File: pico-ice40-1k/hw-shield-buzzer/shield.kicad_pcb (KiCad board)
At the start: 2 copper layers, 53.3 x 53.8 mm, 30 parts, among them J1 JACK_TRS_6PINS, P1 CONN_12, P2 CONN_12, P3 CONN_01X02, SW2 SW_PUSH, U1 TLV320DAC3203, U2 LD39015M18R, U3 TPA2005D1

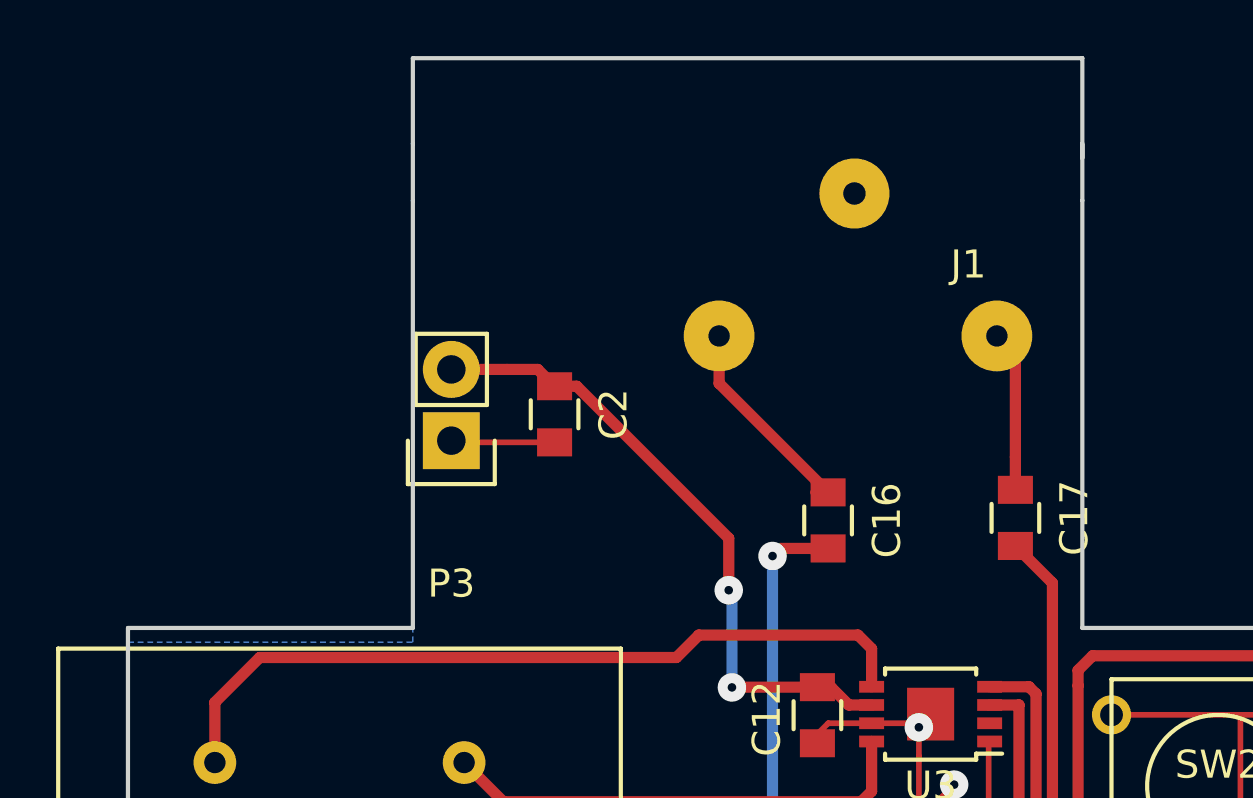
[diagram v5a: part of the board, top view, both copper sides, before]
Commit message: Modif 2 pins header position
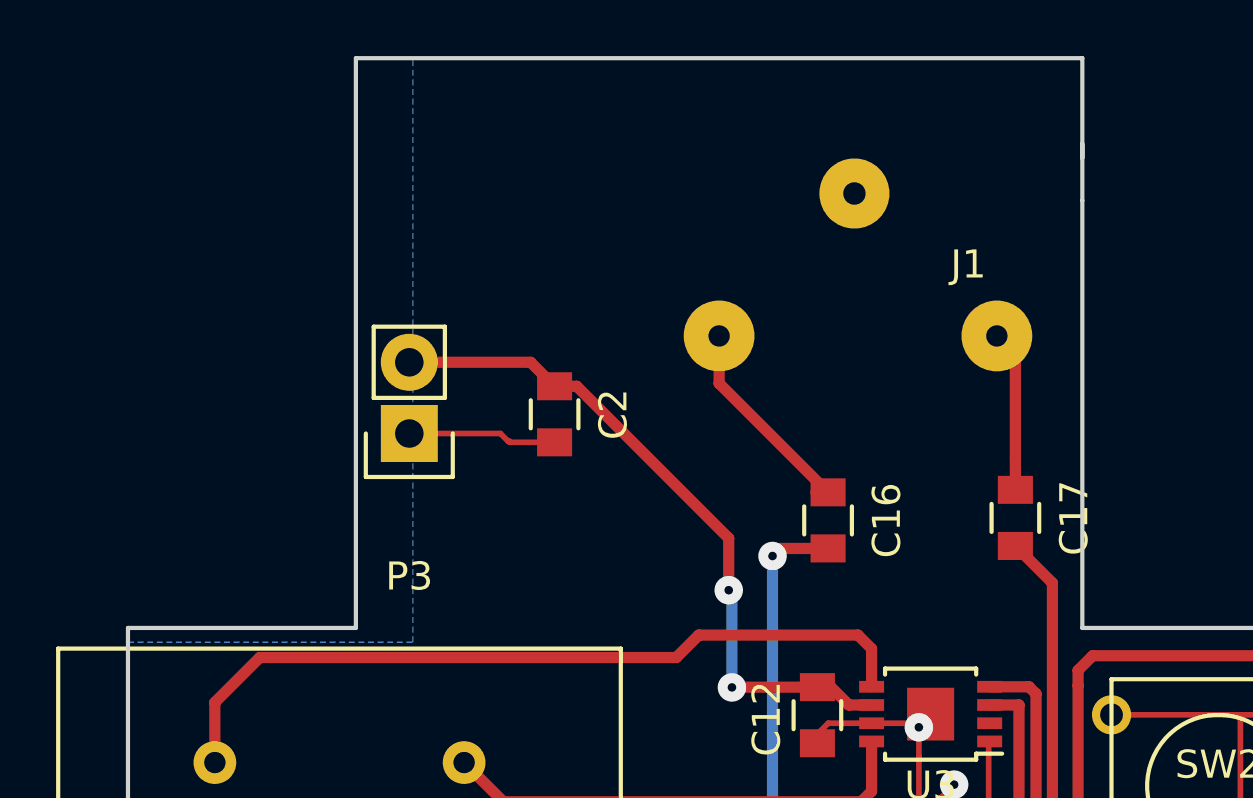
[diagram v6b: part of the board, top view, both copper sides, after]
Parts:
- moved P3 1.52 mm to (155.8, 63.7)
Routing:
- net GND: track 83.5 -> 85.1 mm
- net +5V: track 23.0 -> 24.6 mm
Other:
- outline, holes or cut-outs redrawn
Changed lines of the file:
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@@
   (general
     (links 82)
-    (no_connects 0)
-    (area 145.720999 50.216999 199.211001 104.215001)
+    (no_connects 1)
+    (area 143.079399 48.540599 200.164662 112.781)
     (thickness 1.6)
-    (drawings 16)
-    (tracks 500)
+    (drawings 19)
+    (tracks 502)
     (zones 0)
     (modules 30)
@@
   (layers
     (0 F.Cu signal)
-    (31 B.Cu signal)
+    (31 B.Cu signal hide)
     (32 B.Adhes user)
     (33 F.Adhes user)
@@
     (add_net "Net-(SP1-Pad2)")
   )
+  (module Pin_Headers:Pin_Header_Straight_1x02 locked (layer F.Cu)
+    (at 155.829 63.6778 180)
+    (descr "Through hole pin header")
+    (tags "pin header")
+    (fp_text reference P3 (at 0 -5.1 180) (layer F.SilkS)
+      (effects (font (size 1 1) (thickness 0.15)))
+    )
+    (fp_text value CONN_01X02 (at 0 -3.1 180) (layer F.Fab)
+      (effects (font (size 1 1) (thickness 0.15)))
+    )
+    (fp_line (start 1.27 1.27) (end 1.27 3.81) (layer F.SilkS) (width 0.15))
+    (fp_line (start 1.55 -1.55) (end 1.55 0) (layer F.SilkS) (width 0.15))
+    (fp_line (start -1.75 -1.75) (end -1.75 4.3) (layer F.CrtYd) (width 0.05))
+    (fp_line (start 1.75 -1.75) (end 1.75 4.3) (layer F.CrtYd) (width 0.05))
+    (fp_line (start -1.75 -1.75) (end 1.75 -1.75) (layer F.CrtYd) (width 0.05))
+    (fp_line (start -1.75 4.3) (end 1.75 4.3) (layer F.CrtYd) (width 0.05))
+    (fp_line (start 1.27 1.27) (end -1.27 1.27) (layer F.SilkS) (width 0.15))
+    (fp_line (start -1.55 0) (end -1.55 -1.55) (layer F.SilkS) (width 0.15))
+    (fp_line (start -1.55 -1.55) (end 1.55 -1.55) (layer F.SilkS) (width 0.15))
+    (fp_line (start -1.27 1.27) (end -1.27 3.81) (layer F.SilkS) (width 0.15))
+    (fp_line (start -1.27 3.81) (end 1.27 3.81) (layer F.SilkS) (width 0.15))
+    (pad 1 thru_hole rect (at 0 0 180) (size 2.032 2.032) (drill 1.016) (layers *.Cu *.Mask F.SilkS)
+      (net 2 GND))
+    (pad 2 thru_hole oval (at 0 2.54 180) (size 2.032 2.032) (drill 1.016) (layers *.Cu *.Mask F.SilkS)
+      (net 36 +5V))
+    (model Pin_Headers.3dshapes/Pin_Header_Straight_1x02.wrl
+      (at (xyz 0 -0.05 0))
+      (scale (xyz 1 1 1))
+      (rotate (xyz 0 0 90))
+    )
+  )
   (module Capacitors_SMD:C_0805 placed (layer F.Cu)
     (at 171.45 93.9292)
@@
     )
   )
-  (module Pin_Headers:Pin_Header_Straight_1x02 locked (layer F.Cu)
-    (at 157.3276 63.9318 180)
-    (descr "Through hole pin header")
-    (tags "pin header")
-    (fp_text reference P3 (at 0 -5.1 180) (layer F.SilkS)
-      (effects (font (size 1 1) (thickness 0.15)))
-    )
-    (fp_text value CONN_01X02 (at 0 -3.1 180) (layer F.Fab)
-      (effects (font (size 1 1) (thickness 0.15)))
-    )
-    (fp_line (start 1.27 1.27) (end 1.27 3.81) (layer F.SilkS) (width 0.15))
-    (fp_line (start 1.55 -1.55) (end 1.55 0) (layer F.SilkS) (width 0.15))
-    (fp_line (start -1.75 -1.75) (end -1.75 4.3) (layer F.CrtYd) (width 0.05))
-    (fp_line (start 1.75 -1.75) (end 1.75 4.3) (layer F.CrtYd) (width 0.05))
-    (fp_line (start -1.75 -1.75) (end 1.75 -1.75) (layer F.CrtYd) (width 0.05))
-    (fp_line (start -1.75 4.3) (end 1.75 4.3) (layer F.CrtYd) (width 0.05))
-    (fp_line (start 1.27 1.27) (end -1.27 1.27) (layer F.SilkS) (width 0.15))
-    (fp_line (start -1.55 0) (end -1.55 -1.55) (layer F.SilkS) (width 0.15))
-    (fp_line (start -1.55 -1.55) (end 1.55 -1.55) (layer F.SilkS) (width 0.15))
-    (fp_line (start -1.27 1.27) (end -1.27 3.81) (layer F.SilkS) (width 0.15))
-    (fp_line (start -1.27 3.81) (end 1.27 3.81) (layer F.SilkS) (width 0.15))
-    (pad 1 thru_hole rect (at 0 0 180) (size 2.032 2.032) (drill 1.016) (layers *.Cu *.Mask F.SilkS)
-      (net 2 GND))
-    (pad 2 thru_hole oval (at 0 2.54 180) (size 2.032 2.032) (drill 1.016) (layers *.Cu *.Mask F.SilkS)
-      (net 36 +5V))
-    (model Pin_Headers.3dshapes/Pin_Header_Straight_1x02.wrl
-      (at (xyz 0 -0.05 0))
-      (scale (xyz 1 1 1))
-      (rotate (xyz 0 0 90))
-    )
-  )
   (module Capacitors_SMD:C_0805 (layer F.Cu)
     (at 170.3832 73.7235 270)
@@
     )
   )
-  (gr_line (start 155.956 55.372) (end 155.956 70.612) (angle 90) (layer Edge.Cuts) (width 0.15))
+  (dimension 40.728932 (width 0.3) (layer Eco1.User)
+    (gr_text "40,729 mm" (at 176.165621 41.340258 0.07146336115) (layer Eco1.User)
+      (effects (font (size 1.5 1.5) (thickness 0.3)))
+    )
+    (feature1 (pts (xy 196.5579 63.627) (xy 196.528387 39.964859)))
+    (feature2 (pts (xy 155.829 63.6778) (xy 155.799487 40.015659)))
+    (crossbar (pts (xy 155.802855 42.715657) (xy 196.531755 42.664857)))
+    (arrow1a (pts (xy 196.531755 42.664857) (xy 195.405984 43.252682)))
+    (arrow1b (pts (xy 196.531755 42.664857) (xy 195.404521 42.079842)))
+    (arrow2a (pts (xy 155.802855 42.715657) (xy 156.930089 43.300672)))
+    (arrow2b (pts (xy 155.802855 42.715657) (xy 156.928626 42.127832)))
+  )
+  (dimension 10.2489 (width 0.3) (layer Eco1.User)
+    (gr_text "10,249 mm" (at 212.043 68.77685 90) (layer Eco1.User)
+      (effects (font (size 1.5 1.5) (thickness 0.3)))
+    )
+    (feature1 (pts (xy 196.5325 63.6524) (xy 213.393 63.6524)))
+    (feature2 (pts (xy 196.5325 73.9013) (xy 213.393 73.9013)))
+    (crossbar (pts (xy 210.693 73.9013) (xy 210.693 63.6524)))
+    (arrow1a (pts (xy 210.693 63.6524) (xy 211.279421 64.778904)))
+    (arrow1b (pts (xy 210.693 63.6524) (xy 210.106579 64.778904)))
+    (arrow2a (pts (xy 210.693 73.9013) (xy 211.279421 72.774796)))
+    (arrow2b (pts (xy 210.693 73.9013) (xy 210.106579 72.774796)))
+  )
+  (gr_line (start 196.5325 73.9013) (end 196.5325 63.6778) (angle 90) (layer Eco1.User) (width 0.2))
+  (gr_line (start 202.3364 63.6778) (end 202.3364 63.7032) (angle 90) (layer Eco1.User) (width 0.2))
+  (gr_line (start 155.829 63.6778) (end 202.3364 63.6778) (angle 90) (layer Eco1.User) (width 0.2))
+  (gr_line (start 153.924 50.292) (end 179.832 50.292) (angle 90) (layer Edge.Cuts) (width 0.15))
+  (gr_line (start 153.924 70.612) (end 153.924 50.292) (angle 90) (layer Edge.Cuts) (width 0.15))
+  (gr_line (start 145.796 70.612) (end 153.924 70.612) (angle 90) (layer Edge.Cuts) (width 0.15))
   (gr_line (start 145.796 70.612) (end 145.796 71.12) (angle 90) (layer Edge.Cuts) (width 0.15))
-  (gr_line (start 155.956 70.612) (end 145.796 70.612) (angle 90) (layer Edge.Cuts) (width 0.15))
   (gr_line (start 179.832 50.292) (end 179.832 53.848) (angle 90) (layer Edge.Cuts) (width 0.15))
-  (gr_line (start 155.956 50.292) (end 179.832 50.292) (angle 90) (layer Edge.Cuts) (width 0.15))
-  (gr_line (start 155.956 53.34) (end 155.956 50.292) (angle 90) (layer Edge.Cuts) (width 0.15))
   (gr_line (start 179.832 53.34) (end 179.832 55.372) (angle 90) (layer Edge.Cuts) (width 0.15))
-  (gr_line (start 155.956 55.372) (end 155.956 53.34) (angle 90) (layer Edge.Cuts) (width 0.15))
   (gr_line (start 179.832 70.612) (end 179.832 55.372) (angle 90) (layer Edge.Cuts) (width 0.15))
   (gr_line (start 199.136 70.612) (end 179.832 70.612) (angle 90) (layer Edge.Cuts) (width 0.15))
@@
   (segment (start 179.1393 93.4981) (end 179.1273 93.5101) (width 0.25) (layer F.Cu) (net 1))
   (segment (start 196.6468 74.0156) (end 196.5833 73.9521) (width 0.25) (layer F.Cu) (net 1))
+  (segment (start 155.829 63.6778) (end 159.0802 63.6778) (width 0.2032) (layer F.Cu) (net 2))
+  (segment (start 159.4104 63.9572) (end 159.4104 63.992) (width 0.2032) (layer F.Cu) (net 2))
+  (segment (start 159.3596 63.9572) (end 159.4104 63.9572) (width 0.2032) (layer F.Cu) (net 2))
+  (segment (start 159.0802 63.6778) (end 159.3596 63.9572) (width 0.2032) (layer F.Cu) (net 2))
   (segment (start 181.7393 93.3981) (end 181.7393 92.0981) (width 0.2032) (layer F.Cu) (net 2))
   (segment (start 180.4393 93.3981) (end 181.7393 93.3981) (width 0.2032) (layer F.Cu) (net 2))
@@
   (segment (start 180.8734 78.7908) (end 181.0418 78.7908) (width 0.2032) (layer F.Cu) (net 2))
   (segment (start 181.0418 78.7908) (end 183.4802 81.2292) (width 0.2032) (layer F.Cu) (net 2))
-  (segment (start 161.0106 63.992) (end 157.3878 63.992) (width 0.2032) (layer F.Cu) (net 2))
-  (segment (start 157.3878 63.992) (end 157.3276 63.9318) (width 0.2032) (layer F.Cu) (net 2))
+  (segment (start 161.0106 63.992) (end 159.4104 63.992) (width 0.2032) (layer F.Cu) (net 2))
   (segment (start 173.0662 79.3242) (end 173.0662 78.2668) (width 0.2032) (layer F.Cu) (net 2))
   (segment (start 173.2908 78.0422) (end 174.0027 77.3303) (width 0.2032) (layer F.Cu) (net 2))
@@
   (segment (start 169.2402 90.3478) (end 169.2402 99.6442) (width 0.2032) (layer F.Cu) (net 35))
   (segment (start 170.5483 100.9523) (end 170.5483 101.8921) (width 0.2032) (layer F.Cu) (net 35))
+  (segment (start 155.829 61.1378) (end 160.1564 61.1378) (width 0.4) (layer F.Cu) (net 36))
+  (segment (start 160.1564 61.1378) (end 161.0106 61.992) (width 0.4) (layer F.Cu) (net 36))
   (segment (start 161.0106 61.992) (end 161.8013 61.992) (width 0.4) (layer F.Cu) (net 36))
   (segment (start 167.2209 67.4116) (end 167.2209 69.2658) (width 0.4) (layer F.Cu) (net 36))
   (segment (start 161.8013 61.992) (end 167.2209 67.4116) (width 0.4) (layer F.Cu) (net 36))
-  (segment (start 159.3088 61.3918) (end 160.4104 61.3918) (width 0.4) (layer F.Cu) (net 36))
-  (segment (start 160.4104 61.3918) (end 161.0106 61.992) (width 0.4) (layer F.Cu) (net 36))
-  (segment (start 157.3276 61.3918) (end 159.3088 61.3918) (width 0.4) (layer F.Cu) (net 36))
   (via (at 167.2209 69.2658) (size 1.016) (drill 0.3048) (layers F.Cu B.Cu) (net 36))
   (segment (start 167.3446 72.7235) (end 170.3832 72.7235) (width 0.4) (layer F.Cu) (net 36))
